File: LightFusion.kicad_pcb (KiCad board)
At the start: 4 copper layers, 52.3 x 52.3 mm, 100 parts, among them IC1 MCP3561T-E_ST, IC2 ADS1292IPBSR, J1 303C-C4115-30-04, P1 PHR-2, U1 BMD-350-A-R, U2 TPS7A2033PDBVR, U3 TPS22918DBVR, U4 DRV8837DSGR

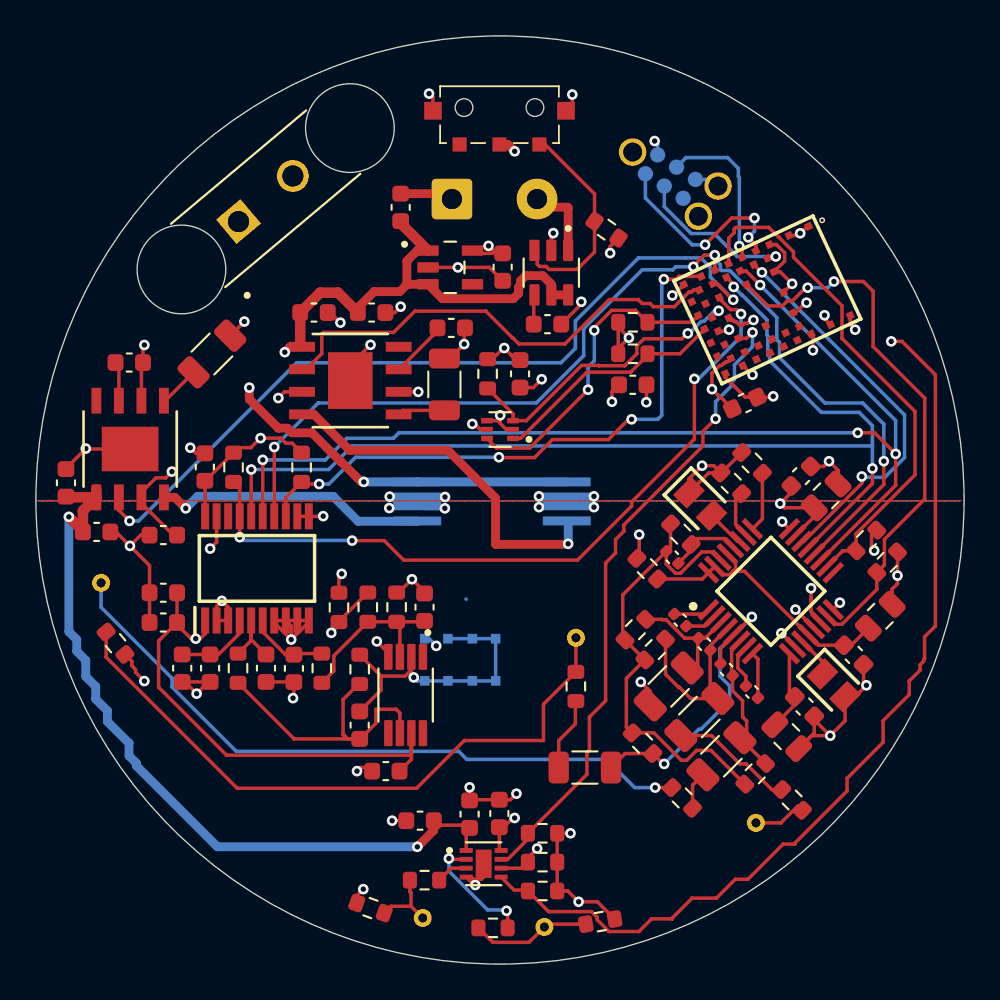
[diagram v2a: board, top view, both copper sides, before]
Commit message: sync with available parts on JLC
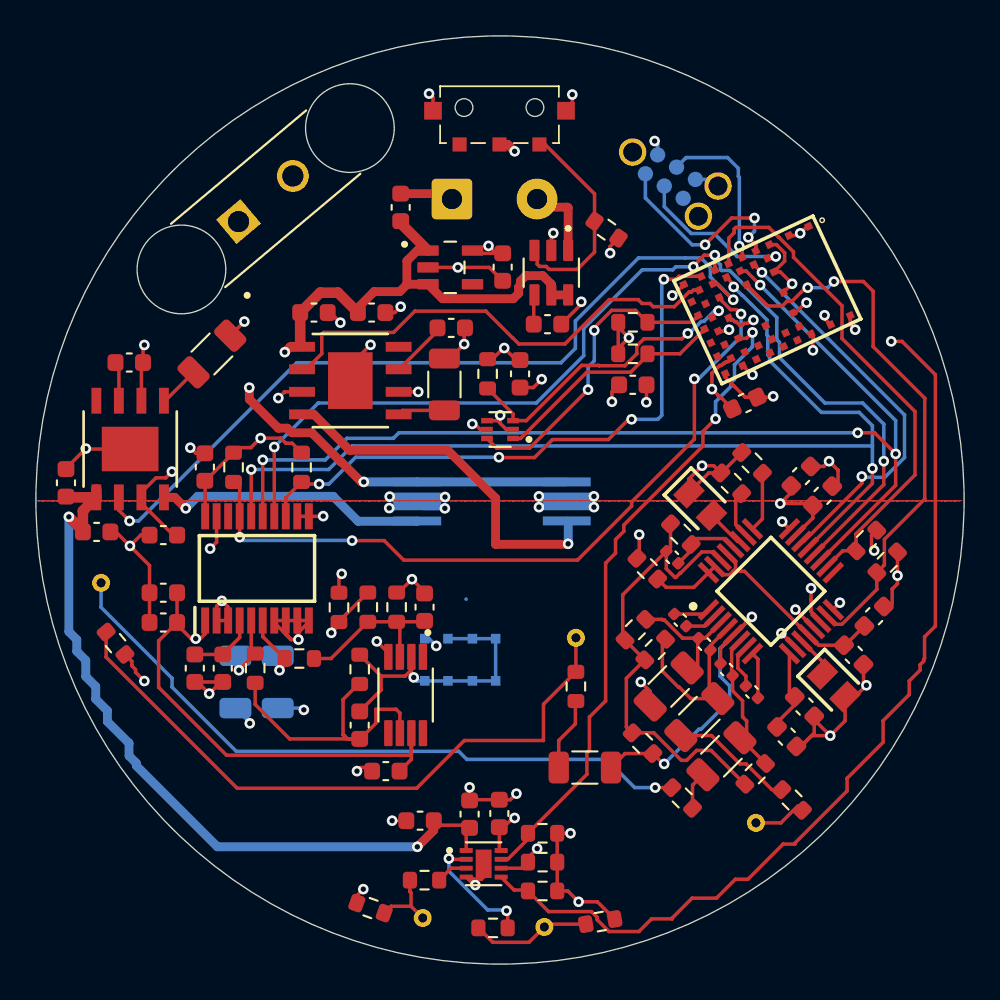
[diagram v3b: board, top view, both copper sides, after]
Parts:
- C_ADC_PHOTO_N1, C_ADC_PHOTO_P1: footprint LightFusion:C_0603_1608Metric -> LightFusion:C_1206_3216Metric; moved to B.Cu
- C_EEG_AVDD_10U1, C_EEG_DVDD_10U1, C_EEG_REF_10U1: footprint LightFusion:C_0805_2012Metric -> LightFusion:C_0603_1608Metric
- moved C_ADC_PHOTO_P1 1.89 mm to (135.1, 140.3)
- moved R_ADC_PHOTO_N1 1.38 mm to (138.7, 138.9), turned to 180 degrees
- moved C_ADC_PHOTO_N1 1.19 mm to (137.5, 140.3)
- moved R_ADC_PHOTO_P1 0.97 mm to (136.2, 139.5)
- moved C_ADC_REF_BYP1 0.71 mm to (134.4, 139.5)
- moved C_ADC_REF_BULK1 0.71 mm to (132.8, 139.5)
- moved C_EEG_AVDD_10U1 0.35 mm to (171.1, 136.6)
- moved C_EEG_DVDD_10U1 0.20 mm to (168.2, 129.8)
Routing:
- net /PD_ADC/3V3_A: track 42.3 -> 40.8 mm
- net /PD_ADC/PHOTO_BIAS: track 9.79 -> 9.17 mm
- net /PD_ADC/ADC_VREF: track 4.46 -> 3.88 mm
- net GND: track 141.9 -> 142.3 mm, vias 62 -> 63
- net /PD_ADC/ADC_PHOTO_N: track 4.53 -> 4.29 mm, vias 0 -> 1
- net /PD_ADC/ADC_PHOTO_P: track 4.43 -> 4.21 mm, vias 0 -> 1

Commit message: redesigned MCU part to be able to solder with iron
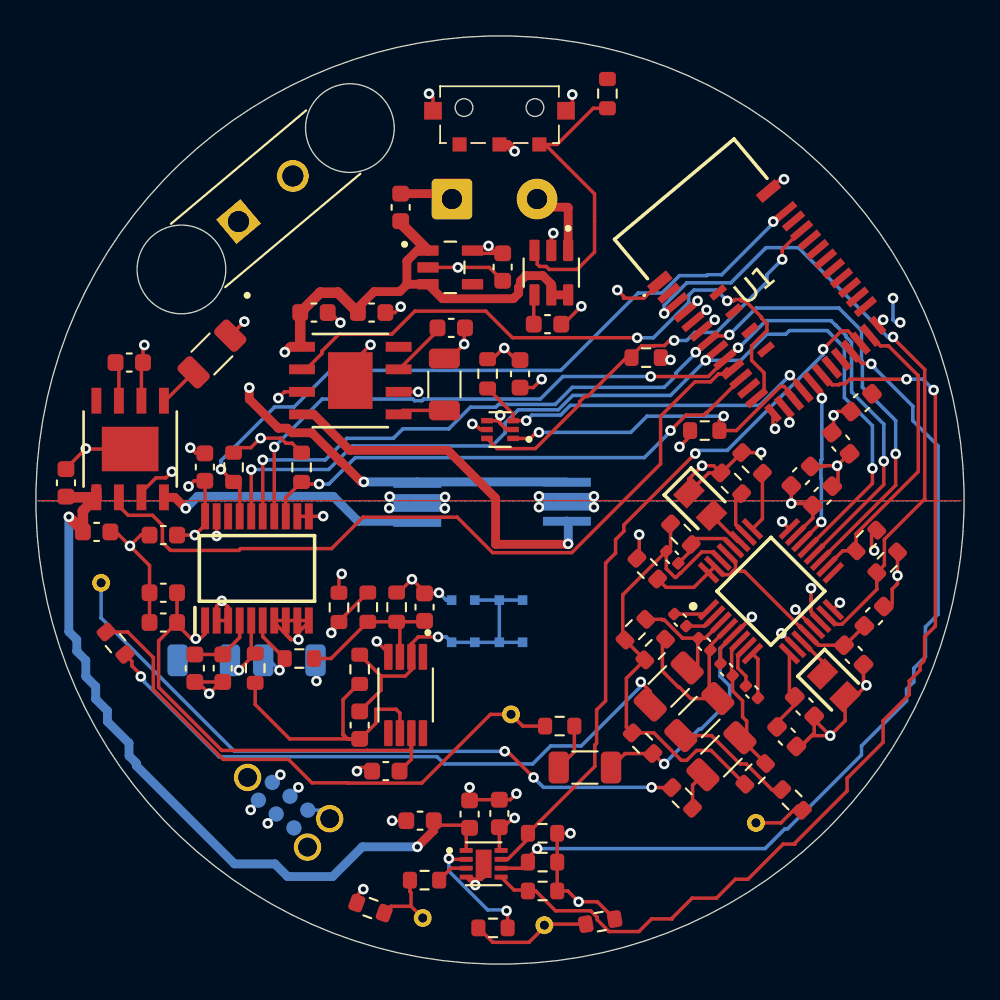
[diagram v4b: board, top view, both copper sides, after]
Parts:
- U1: value BMD-350-A-R -> MDBT42-512KV2; footprint LightFusion:BMD-350 -> LightFusion:MDBT42512KV2
- moved J_PROG1 41.6 mm to (137.8, 147.2), turned to -38 degrees
- moved C_M2 12.9 mm to (170.4, 124.5), turned to 40 degrees
- moved R_ON_PD1 7.67 mm to (156.1, 107.1), turned to -90 degrees
- moved R1 5.93 mm to (161.5, 126.1)
- moved C_M1 5.87 mm to (169.2, 126.8), turned to -50 degrees
- moved E_EEG3 5.66 mm to (150.6, 142.1)
- moved D_PD1 2.65 mm to (149.3, 136.8)
- moved R_EEG_PROT_N2 2.42 mm to (153.4, 142.7), turned to 0 degrees
- moved C_ADC_PHOTO_P1 2.16 mm to (133.3, 139.0), turned to 180 degrees
- moved R2 2.13 mm to (158.2, 122.0), turned to 180 degrees
- moved C_ADC_PHOTO_N1 1.39 mm to (138.1, 139.0), turned to 0 degrees
- moved U1 1.26 mm to (164.3, 117.8), turned to 40 degrees
- moved STIM_E_P1 0.10 mm to (152.5, 154.0)
- moved D_730 0.09 mm to (145.3, 130.2)
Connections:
- U1 pad 10: ADC_MISO -> PWM_730
- U1 pad 11: ADC_SCK -> ADC_CS_N
- U1 pad 12: PWM_730 -> unconnected-(U1-P0.10-Pad12)
- U1 pad 13: ADC_CS_N -> PWM_850
- U1 pad 14: PWM_850 -> GND
- U1 pad 15: GND -> 3V3_DIG
- U1 pad 16: unconnected-(U1-P0.09-Pad16) -> I2C_TEMP_SCL
- U1 pad 17: unconnected-(U1-P0.10-Pad17) -> TEMP_ALERT
- U1 pad 18: I2C_TEMP_SDA -> /EEG_DRDY
- U1 pad 19: TEMP_ALERT -> /MCU_STIM_IN2
- U1 pad 2: GND -> unconnected-(U1-P0.23-Pad2)
- U1 pad 20: I2C_TEMP_SCL -> unconnected-(U1-P0.00/XL1-Pad20)
- U1 pad 21: /MCU_STIM_IN2 -> unconnected-(U1-P0.01/XL2-Pad21)
- U1 pad 22: unconnected-(U1-P0.07-Pad22) -> /MCU_STIM_IN1
- U1 pad 23: unconnected-(U1-P0.01-Pad23) -> /MCU_STIM_EN
- U1 pad 24: unconnected-(U1-P0.00-Pad24) -> /EEG_CS_N
- U1 pad 25: 3V3_DIG -> GND
- U1 pad 26: GND -> unconnected-(U1-DCC-Pad26)
- U1 pad 27: /MCU_STIM_IN1 -> unconnected-(U1-DEC4-Pad27)
- U1 pad 3: GND -> /EEG_RESET_N
- U1 pad 34: unconnected-(U1-P0.26-Pad34) -> I2C_TEMP_SDA
- U1 pad 36: unconnected-(U1-P0.24-Pad36) -> ADC_DRDY_N
- U1 pad 38: GND -> unconnected-(U1-P0.24-Pad38)
- U1 pad 39: GND -> unconnected-(U1-P0.20-Pad39)
- U1 pad 40: GND -> unconnected-(U1-P0.16-Pad40)
- U1 pad 41: /EEG_RESET_N -> unconnected-(U1-P0.14-Pad41)
- U1 pad 6: /EEG_DRDY -> /RESET
- U1 pad 7: /RESET -> ADC_MOSI
- U1 pad 8: ADC_MOSI -> ADC_MISO
- U1 pad 9: /EEG_CS_N -> ADC_SCK
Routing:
- net /SWDCLK: track 9.12 -> 83.7 mm, vias 1 -> 4
- net /SWDIO: track 11.4 -> 84.8 mm, vias 3 -> 2
- net /RESET: track 9.10 -> 79.4 mm, vias 1 -> 2
- net /EEG_DRDY: track 22.4 -> 9.82 mm
- net /EEG_CS_N: track 29.1 -> 17.0 mm
- net GND: track 142.3 -> 131.1 mm, vias 63 -> 56
- net PWM_850: track 27.2 -> 36.0 mm, vias 0 -> 2
- net /MCU_STIM_IN2: track 63.2 -> 55.8 mm
- net I2C_TEMP_SDA: track 17.7 -> 24.5 mm
- net /EEG_RESET_N: track 31.4 -> 37.7 mm
- net Net-(E_EEG3-Pad1): track 36.9 -> 31.2 mm
- net I2C_TEMP_SCL: track 13.4 -> 18.9 mm, vias 0 -> 2
- net /MCU_STIM_IN1: track 55.5 -> 50.0 mm
- net ADC_MISO: track 59.7 -> 54.4 mm
- net ADC_MOSI: track 61.9 -> 56.7 mm
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
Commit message: final version with bom and placement
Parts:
- renumbered C_EEG_AC_N1 to C1, C_EEG_DVDD_100N1 to C10, C_EEG_PGA1 to C11, C_EEG_PGA2 to C12, C_EEG_REF_10U1 to C13, C_EEG_REF_100N1 to C14, C_EEG_RLD_FB1 to C15, C_EEG_VCAP1 to C16, C_EEG_VCAP2 to C17, C_M1 to C18, C_M2 to C19, C_EEG_AC_N2 to C2, C_STIM_VCC1 to C20, C_STIM_VM1 to C21, C_STIM_VM2 to C22, C_PWR3 to C23, C_PWR4 to C24, C_PWR_SW_CT1 to C25, C730_BULK1 to C26, C730_BYP1 to C27, C850_BULK1 to C28, C850_BYP1 to C29, C_EEG_AC_P1 to C3, CSLOPE_730 to C30, CSLOPE_850 to C31, C_TEMP1 to C32, C_ADC_AVDD_BULK1 to C33, C_ADC_AVDD_BYP1 to C34, C_ADC_DVDD_BULK1 to C35, C_ADC_DVDD_BYP1 to C36, C_ADC_PHOTO_N1 to C37, C_ADC_PHOTO_P1 to C38, C_ADC_REF_BULK1 to C39, C_EEG_AC_P2 to C4, C_ADC_REF_BYP1 to C40, C_PD_BIAS1 to C41, C_PD_FB1 to C42, C_PD_TIA_SUPPLY1 to C43, C_EEG_AVDD_10U1 to C5, C_EEG_AVDD_100N1 to C6, C_EEG_DIFF1 to C7, C_EEG_DIFF2 to C8, C_EEG_DVDD_10U1 to C9, D_730 to D1, D_850 to D2, D_PD1 to D3, E_EEG1 to E1, E_EEG2 to E2, E_EEG3 to E3, STIM_E_N1 to E4, STIM_E_P1 to E5, J_PROG1 to J2, R_EEG_PROT_N1 to R10, R_EEG_PROT_N2 to R11, R_EEG_PROT_P1 to R12, R_EEG_PROT_P2 to R13, R_EEG_RESET_PD1 to R14, R_EEG_RLD_FB1 to R15, R_EEG_SUPPLY_A1 to R16, R_SLEEP_PD1 to R17, R_STIM_IN1 to R18, R_STIM_IN2 to R19, R_STIM_N1 to R20, R_STIM_P1 to R21, R_STIM_PD1 to R22, R_STIM_PD2 to R23, R_ON_PD1 to R24, RFB_730 to R25, RFB_850 to R26, R_TEMP_ALERT1 to R27, R_ADC_CS_PU1 to R28, R_ADC_IRQ_PU1 to R29, R_EEG_BIAS_N1 to R3, R_ADC_PHOTO_N1 to R30, R_ADC_PHOTO_P1 to R31, R_PD_BIAS_BOT1 to R32, R_PD_BIAS_TOP1 to R33, R_PD_FB1 to R34, R_PD_SUPPLY1 to R35, R_EEG_BIAS_N2 to R4, R_EEG_BIAS_P1 to R5, R_EEG_BIAS_P2 to R6, R_EEG_CS_PU1 to R7, R_EEG_GPIO1 to R8, R_EEG_GPIO2 to R9, U_PD_TIA1 to U10, IC2 to U5, U_LED730 to U6, U_LED850 to U7, U_TEMP1 to U8, IC1 to U9
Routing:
- net /Power/PWR_ON: track 16.8 -> 12.8 mm
- net GND: track 131.1 -> 130.1 mm, vias 56 -> 70
- net /Power/BAT+: track 22.2 -> 21.7 mm
